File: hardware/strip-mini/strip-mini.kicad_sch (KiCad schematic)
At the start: 27 parts, among them J101 CORTEX-DEBUG, J102 JAE_DX07S016JA3, SW101 SW_Push, U101 AP2112K-3.3, U102 ATSAMD51G, Y101 32k768

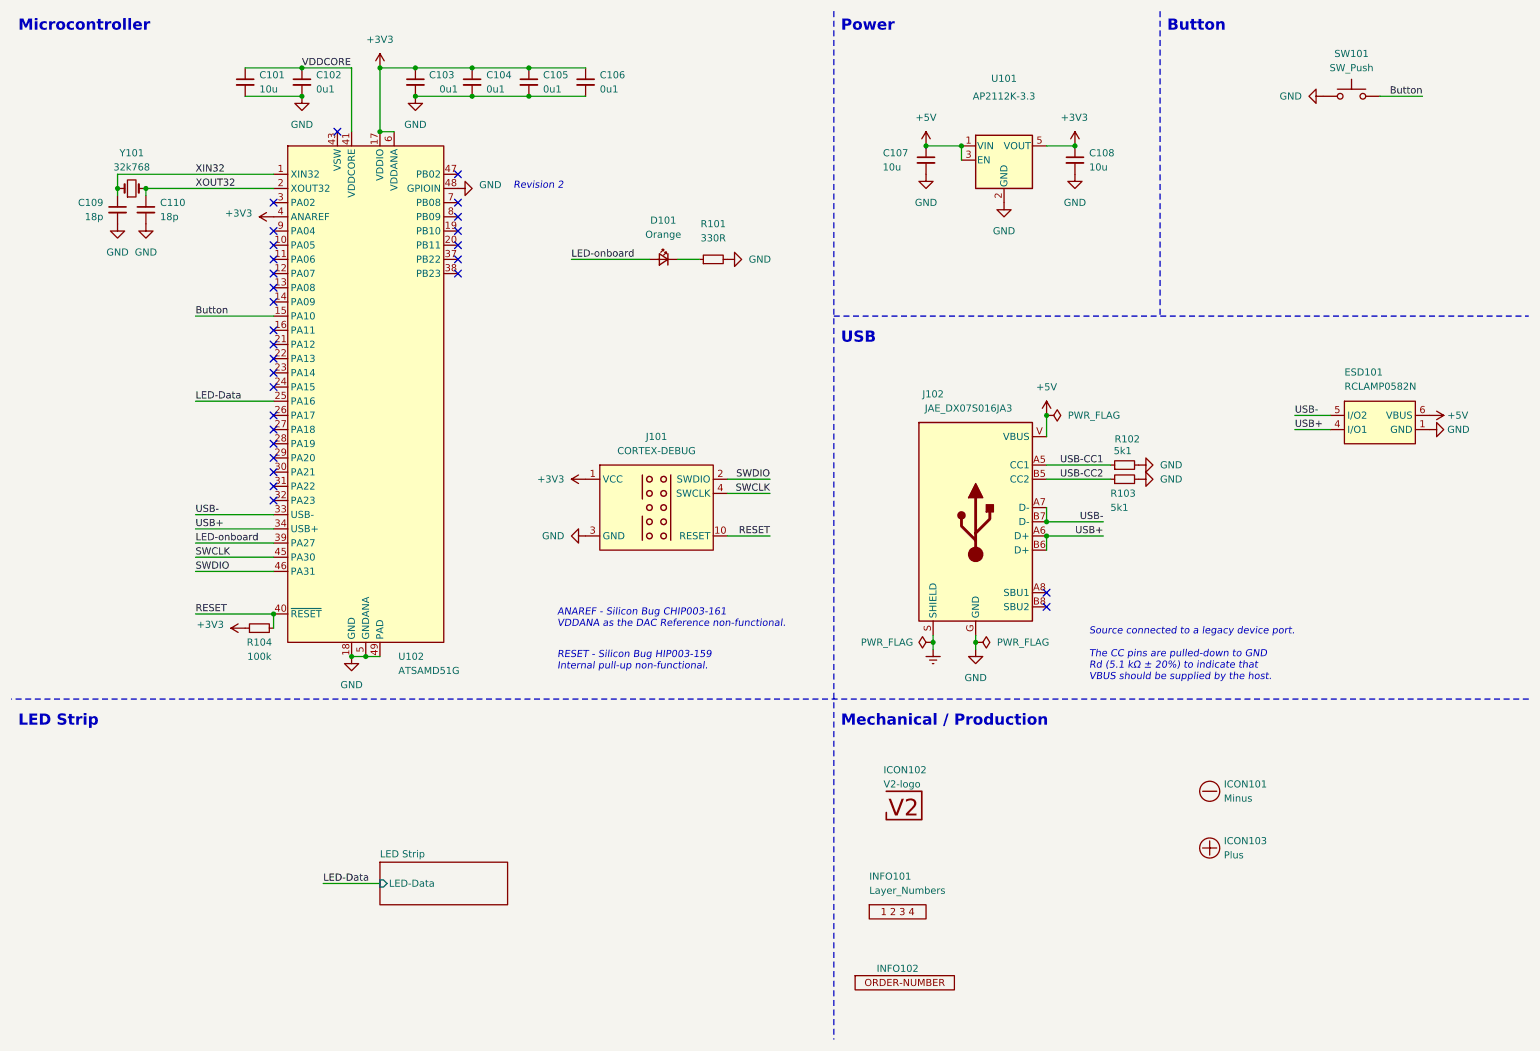
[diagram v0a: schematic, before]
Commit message: Replace Order_Number
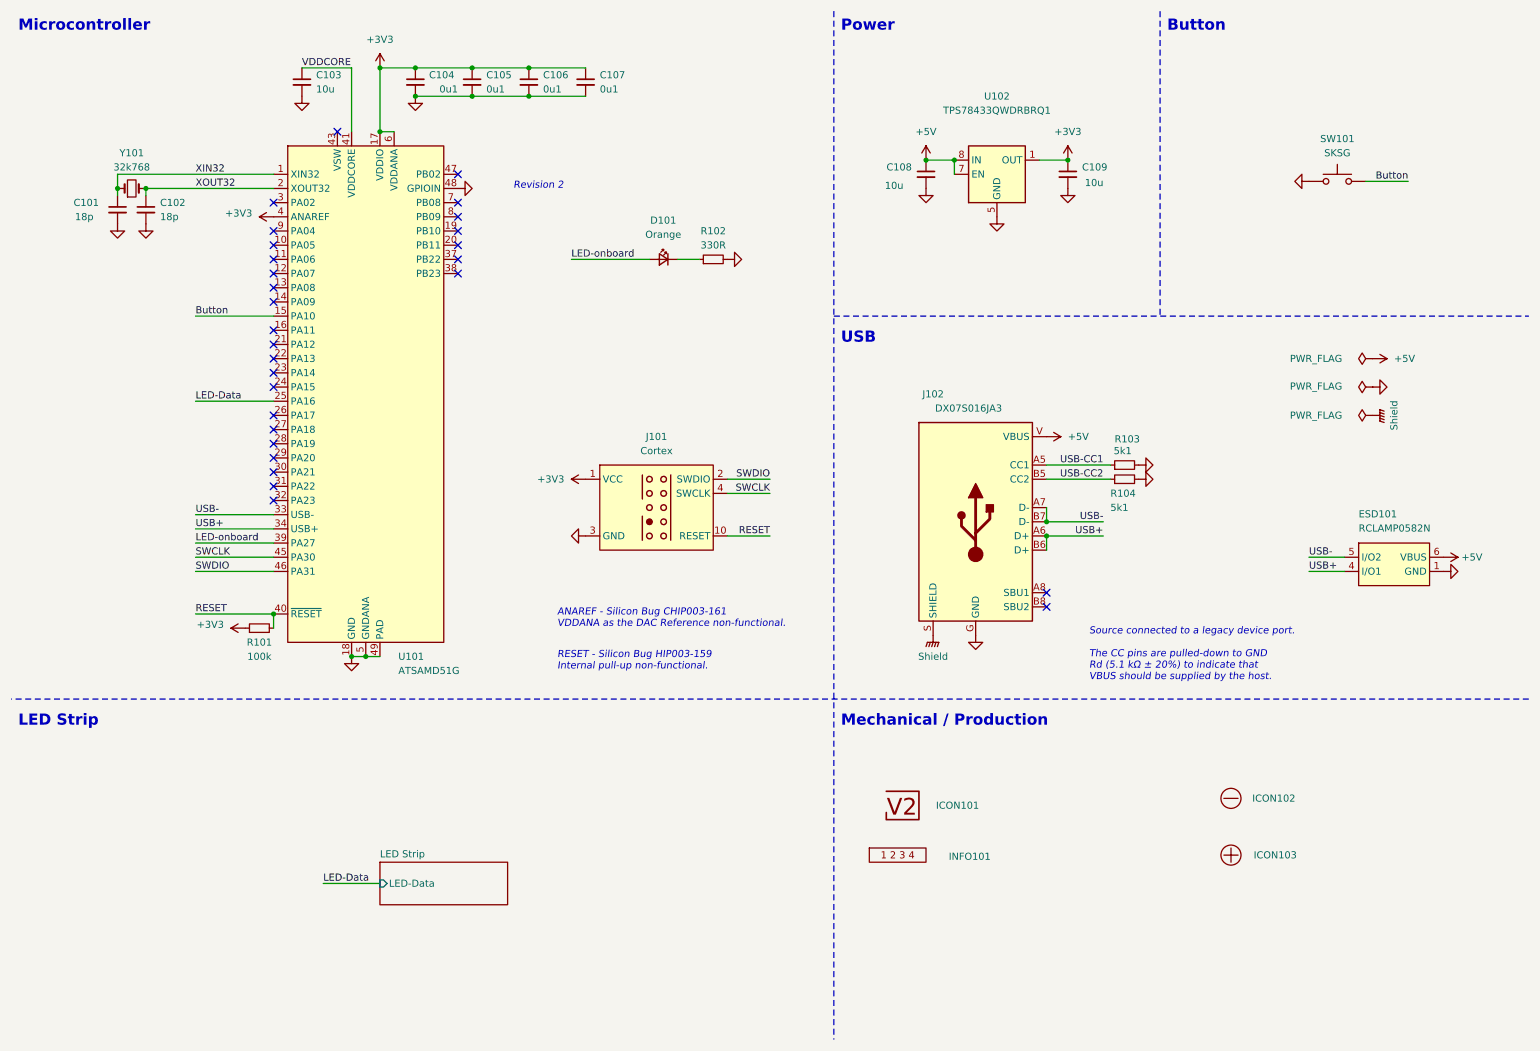
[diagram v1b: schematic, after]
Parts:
- removed C102: 0u1, Capacitor_SMD:C_0603_1608Metric, symbol Device:C_Small
- removed C107, C108: 10u, Capacitor_SMD:C_0603_1608Metric, symbol Device:C_Small
- removed INFO102: ORDER-NUMBER, V2_Production:Order_Number, symbol V2_Production:Order_Number
- removed U101: AP2112K-3.3, Package_TO_SOT_SMD:SOT-23-5, symbol Regulator_Linear:AP2112K-3.3
- added C108, C109: 10u, V2_Capacitor_SMD:C_0805, symbol V2_Device:C_0805_10u
- added U102: TPS78433QWDRBRQ1, V2_Package_SON:VSON-8-1_3x3mm_P0.65_EP1.65x2.4mm, symbol V2_Regulator_Linear:TPS78433QWDRBRQ1
- C101: renamed from C109; footprint Capacitor_SMD:C_0603_1608Metric -> V2_Capacitor_SMD:C_0603; symbol Device:C_Small -> V2_Device:C_0603_18p; Manufacturer (none) -> YAGEO; Mouser (none) -> 603-CC603JRNPO9BN180; Product (none) -> CC0603JRNPO9BN180
- C102: renamed from C110; footprint Capacitor_SMD:C_0603_1608Metric -> V2_Capacitor_SMD:C_0603; symbol Device:C_Small -> V2_Device:C_0603_18p; Manufacturer (none) -> YAGEO; Mouser (none) -> 603-CC603JRNPO9BN180; Product (none) -> CC0603JRNPO9BN180
- C103: renamed from C101; footprint Capacitor_SMD:C_0603_1608Metric -> V2_Capacitor_SMD:C_0603; symbol Device:C_Small -> V2_Device:C_0603_10u; Manufacturer (none) -> TDK; Mouser (none) -> 810-C1608X6S1A106M; Product (none) -> C1608X6S1A106M080AC; Rating (none) -> 10V
- C104: renamed from C103; footprint Capacitor_SMD:C_0603_1608Metric -> V2_Capacitor_SMD:C_0603; symbol Device:C_Small -> V2_Device:C_0603_0u1; Manufacturer (none) -> TDK; Mouser (none) -> 810-CGA3E2X7R1H104MA; Product (none) -> CGA3E2X7R1H104M080AA; Rating (none) -> 50V
- C105: renamed from C104; footprint Capacitor_SMD:C_0603_1608Metric -> V2_Capacitor_SMD:C_0603; symbol Device:C_Small -> V2_Device:C_0603_0u1; Manufacturer (none) -> TDK; Mouser (none) -> 810-CGA3E2X7R1H104MA; Product (none) -> CGA3E2X7R1H104M080AA; Rating (none) -> 50V
- C106: renamed from C105; footprint Capacitor_SMD:C_0603_1608Metric -> V2_Capacitor_SMD:C_0603; symbol Device:C_Small -> V2_Device:C_0603_0u1; Manufacturer (none) -> TDK; Mouser (none) -> 810-CGA3E2X7R1H104MA; Product (none) -> CGA3E2X7R1H104M080AA; Rating (none) -> 50V
- C107: renamed from C106; footprint Capacitor_SMD:C_0603_1608Metric -> V2_Capacitor_SMD:C_0603; symbol Device:C_Small -> V2_Device:C_0603_0u1; Manufacturer (none) -> TDK; Mouser (none) -> 810-CGA3E2X7R1H104MA; Product (none) -> CGA3E2X7R1H104M080AA; Rating (none) -> 50V
- D101: footprint LED_SMD:LED_0603_1608Metric -> V2_LED:LED_0603; symbol Device:LED_Small -> V2_Device:LED_0603_Orange; Manufacturer (none) -> ROHM Semiconductor; Mouser (none) -> 755-SML-D12D1WT86; Product (none) -> SML-D12D1WT86
- ESD101: Manufacturer (none) -> Semtech; Mouser (none) -> 947-RCLAMP0582N.TCT; Product (none) -> RCLAMP0582N.TCT
- ICON101: renamed from ICON102; symbol V2_Artwork:V2-logo -> V2_Artwork:V2-logo-tiny
- J101: value CORTEX-DEBUG -> Cortex; footprint V2_Cortex_Debug:Cortex_Debug_Pad -> V2_Connector_Debug:Cortex; symbol V2_Cortex_Debug:Cortex_Debug -> V2_Connector_Debug:Cortex
- J102: value JAE_DX07S016JA3 -> DX07S016JA3; Manufacturer (none) -> JAE Electronics; Mouser (none) -> 656-DX07S016JA3R1500; Product (none) -> DX07S016JA3R1500
- R101: renamed from R104; footprint Resistor_SMD:R_0603_1608Metric -> V2_Resistor_SMD:R_0603; symbol Device:R_Small -> V2_Device:R_0603_100k; Manufacturer (none) -> Vishay; Mouser (none) -> 71-CRCW0603100KFKEAC; Product (none) -> CRCW0603100KFKEAC; Rating (none) -> 100mW
- R102: renamed from R101; footprint Resistor_SMD:R_0603_1608Metric -> V2_Resistor_SMD:R_0603; symbol Device:R_Small -> V2_Device:R_0603_330R; Manufacturer (none) -> Vishay; Mouser (none) -> 71-CRCW0603330RFKEAC; Product (none) -> CRCW0603330RFKEAC; Rating (none) -> 100mW
- R103: renamed from R102; footprint Resistor_SMD:R_0603_1608Metric -> V2_Resistor_SMD:R_0603; symbol Device:R_Small -> V2_Device:R_0603_5k1; Manufacturer (none) -> Vishay; Mouser (none) -> 71-CRCW06035K10FKEAC; Product (none) -> CRCW06035K10FKEAC; Rating (none) -> 100mW
- R104: renamed from R103; footprint Resistor_SMD:R_0603_1608Metric -> V2_Resistor_SMD:R_0603; symbol Device:R_Small -> V2_Device:R_0603_5k1; Manufacturer (none) -> Vishay; Mouser (none) -> 71-CRCW06035K10FKEAC; Product (none) -> CRCW06035K10FKEAC; Rating (none) -> 100mW
- SW101: value SW_Push -> SKSG; symbol Switch:SW_Push -> V2_Switch:SKSG; Manufacturer (none) -> Alps Alpine; Mouser (none) -> 688-SKSGACE010; Product (none) -> SKSGACE010
- U101: renamed from U102; Manufacturer (none) -> Microchip Technology; Mouser (none) -> 556-ATSAMD51G19AMU; Product (none) -> ATSAMD51G19A-MU
- Y101: symbol Device:Crystal_Small -> V2_Device:Crystal_3.2x1.5_32k768; Manufacturer (none) -> ABRACON; Mouser (none) -> 815-ABS0716632.768KT; Product (none) -> ABS07-166-32.768KHZ-T
- renumbered ICON101 to ICON102
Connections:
- net +3V3: now also C109.1, U102.1 (OUT)
- net +5V: now also C108.1, U102.7 (EN), U102.8 (IN)
- net GND: now also C108.2, C109.2, U102.5 (GND), U102.9 (GND)
- net Earth renamed Shield
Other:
- moved on the sheet: C103, ESD101, ICON102, ICON103, INFO101, SW101

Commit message: Update Library
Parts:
- C101, C102: symbol V2_Device:C_0603_18p -> V2_Capacitor:0603_18p
- C103: symbol V2_Device:C_0603_10u -> V2_Capacitor:0603_10u
- C104, C105, C106, C107: symbol V2_Device:C_0603_0u1 -> V2_Capacitor:0603_0u1
- C108, C109: symbol V2_Device:C_0805_10u -> V2_Capacitor:0805_10u
- D101: symbol V2_Device:LED_0603_Orange -> V2_LED:0603_Orange
- R101: symbol V2_Device:R_0603_100k -> V2_Resistor:0603_100k
- R102: symbol V2_Device:R_0603_330R -> V2_Resistor:0603_330R
- R103, R104: symbol V2_Device:R_0603_5k1 -> V2_Resistor:0603_5k1
- Y101: symbol V2_Device:Crystal_3.2x1.5_32k768 -> V2_Crystal:3.2x1.5_32k768

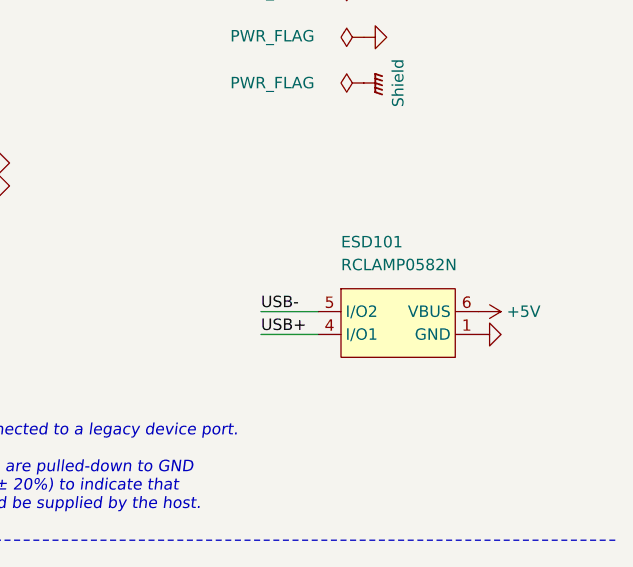
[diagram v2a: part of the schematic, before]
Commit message: Update ESD suppressor
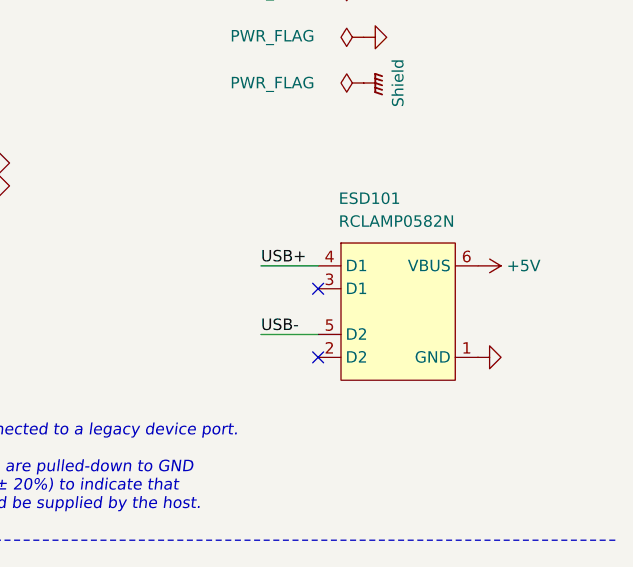
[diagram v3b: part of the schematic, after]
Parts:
- C101, C102: Manufacturer YAGEO -> TDK; Mouser 603-CC603JRNPO9BN180 -> 810-CGA3E2C0G1H180J; Product CC0603JRNPO9BN180 -> CGA3E2C0G1H180J080AA
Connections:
- no-connect marks 29 -> 31
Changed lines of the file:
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@@
 	(title_block
 		(title "V2 strip mini")
-		(date "2026-02-11")
+		(date "2026-03-14")
 		(rev "2026-02-11")
 		(company "Versio Duo")
@@
 	)
 	(no_connect
+		(at 251.46 115.57)
+	)
+	(no_connect
+		(at 251.46 107.95)
+	)
+	(no_connect
 		(at 71.12 34.29)
 	)
@@
 	(wire
 		(pts
-			(xy 245.11 110.49) (xy 251.46 110.49)
+			(xy 245.11 113.03) (xy 251.46 113.03)
 		)
 		(stroke
@@
 		)
 	)
+	(wire
+		(pts
+			(xy 245.11 105.41) (xy 251.46 105.41)
+		)
+		(stroke
+			(width 0)
+			(type default)
+		)
+	)
 	(polyline
 		(pts
@@
 	(wire
 		(pts
-			(xy 245.11 113.03) (xy 251.46 113.03)
-		)
-		(stroke
-			(width 0)
-			(type default)
-		)
-	)
-	(wire
-		(pts
 			(xy 113.03 57.15) (xy 127 57.15)
 		)
@@
 	)
 	(label "USB+"
+		(at 245.11 105.41 0)
+		(effects
+			(font
+				(size 1.27 1.27)
+			)
+			(justify left bottom)
+		)
+	)
+	(label "USB+"
 		(at 45.72 105.41 0)
 		(effects
@@
 		)
 	)
-	(label "USB+"
-		(at 245.11 113.03 0)
-		(effects
-			(font
-				(size 1.27 1.27)
-			)
-			(justify left bottom)
-		)
-	)
 	(label "SWDIO"
 		(at 148.59 96.52 180)
@@
 	)
 	(label "USB-"
-		(at 245.11 110.49 0)
+		(at 245.11 113.03 0)
 		(effects
 			(font
@@
 			)
 		)
-		(property "Description" "Resistor, small symbol"
+		(property "Description" ""
 			(at 224.79 93.98 0)
 			(effects
@@
 			)
 		)
-		(property "Description" "Unpolarized capacitor, small symbol"
+		(property "Description" ""
 			(at 115.57 38.1 0)
 			(effects
@@
 		(dnp no)
 		(property "Reference" "ESD101"
-			(at 254 103.505 0)
+			(at 253.746 98.679 0)
 			(effects
 				(font
@@
 		)
 		(property "Value" "RCLAMP0582N"
-			(at 254 106.045 0)
+			(at 253.746 101.219 0)
 			(effects
 				(font
@@
 			)
 		)
-		(property "Description" "Push button switch, generic, two pins"
+		(property "Description" "Push button"
 			(at 250.19 43.18 0)
 			(effects
@@
 	(symbol
 		(lib_id "V2_power:+5V")
-		(at 269.24 110.49 270)
+		(at 269.24 105.41 270)
 		(unit 1)
 		(exclude_from_sim no)
@@
 		(fields_autoplaced yes)
 		(property "Reference" "#PWR127"
-			(at 265.43 110.49 0)
+			(at 265.43 105.41 0)
 			(effects
 				(font
@@
 		)
 		(property "Value" "+5V"
-			(at 272.415 110.4899 90)
+			(at 272.415 105.4099 90)
 			(effects
 				(font
@@
 		)
 		(property "Footprint" ""
-			(at 269.24 110.49 0)
+			(at 269.24 105.41 0)
 			(effects
 				(font
@@
 		)
 		(property "Datasheet" ""
-			(at 269.24 110.49 0)
+			(at 269.24 105.41 0)
 			(effects
 				(font
@@
 		)
 		(property "Description" ""
-			(at 269.24 110.49 0)
+			(at 269.24 105.41 0)
 			(effects
 				(font
@@
 			)
 		)
-		(property "Description" "Light emitting diode, small symbol"
+		(property "Description" ""
 			(at 129.54 57.15 0)
 			(effects
@@
 			)
 		)
-		(property "Description" "Unpolarized capacitor, small symbol"
+		(property "Description" ""
 			(at 176.53 55.372 0)
 			(effects
@@
 			)
 		)
-		(property "Description" "Two pin crystal, small symbol"
+		(property "Description" ""
 			(at 34.29 44.45 0)
 			(effects
@@
 			)
 		)
-		(property "Description" "Unpolarized capacitor, small symbol"
+		(property "Description" ""
 			(at 36.83 62.738 0)
 			(effects
@@
 			)
 		)
-		(property "Mouser" "603-CC603JRNPO9BN180"
+		(property "Mouser" "810-CGA3E2C0G1H180J"
 			(at 36.83 71.628 0)
 			(effects
@@
 			)
 		)
-		(property "Product" "CC0603JRNPO9BN180"
+		(property "Product" "CGA3E2C0G1H180J080AA"
 			(at 36.83 68.834 0)
 			(effects
@@
 			)
 		)
-		(property "Manufacturer" "YAGEO"
+		(property "Manufacturer" "TDK"
 			(at 36.83 66.04 0)
 			(effects
@@
 			)
 		)
-		(property "Description" "Unpolarized capacitor, small symbol"
+		(property "Description" ""
 			(at 64.77 40.64 0)
 			(effects
@@
 			)
 		)
-		(property "Description" "Unpolarized capacitor, small symbol"
+		(property "Description" ""
 			(at 31.75 62.738 0)
 			(effects
@@
 			)
 		)
-		(property "Mouser" "603-CC603JRNPO9BN180"
+		(property "Mouser" "810-CGA3E2C0G1H180J"
 			(at 31.75 71.628 0)
 			(effects
@@
 			)
 		)
-		(property "Product" "CC0603JRNPO9BN180"
+		(property "Product" "CGA3E2C0G1H180J080AA"
 			(at 31.75 68.834 0)
 			(effects
@@
 			)
 		)
-		(property "Manufacturer" "YAGEO"
+		(property "Manufacturer" "TDK"
 			(at 31.75 66.04 0)
 			(effects
@@
 			)
 		)
-		(property "Description" "Resistor, small symbol"
+		(property "Description" ""
 			(at 151.13 57.15 0)
 			(effects
@@
 	(symbol
 		(lib_id "V2_power:GND")
-		(at 269.24 113.03 90)
+		(at 269.24 115.57 90)
 		(unit 1)
 		(exclude_from_sim no)
@@
 		(fields_autoplaced yes)
 		(property "Reference" "#PWR128"
-			(at 275.59 113.03 0)
+			(at 275.59 115.57 0)
 			(effects
 				(font
@@
 		)
 		(property "Value" "GND"
-			(at 272.415 113.0299 90)
+			(at 272.415 115.5699 90)
 			(effects
 				(font
@@
 		)
 		(property "Footprint" ""
-			(at 269.24 113.03 0)
+			(at 269.24 115.57 0)
 			(effects
 				(font
@@
 		)
 		(property "Datasheet" ""
-			(at 269.24 113.03 0)
+			(at 269.24 115.57 0)
 			(effects
 				(font
@@
 		)
 		(property "Description" ""
-			(at 269.24 113.03 0)
+			(at 269.24 115.57 0)
 			(effects
 				(font
@@
 			)
 		)
-		(property "Description" "Unpolarized capacitor, small symbol"
+		(property "Description" ""
 			(at 105.41 38.1 0)
 			(effects
@@
 			)
 		)
-		(property "Description" "Unpolarized capacitor, small symbol"
+		(property "Description" ""
 			(at 201.93 55.372 0)
 			(effects
@@
 			)
 		)
-		(property "Description" "Unpolarized capacitor, small symbol"
+		(property "Description" ""
 			(at 85.09 38.1 0)
 			(effects
@@
 			)
 		)
-		(property "Description" "Resistor, small symbol"
+		(property "Description" ""
 			(at 224.79 96.52 0)
 			(effects
@@
 			)
 		)
-		(property "Description" "Unpolarized capacitor, small symbol"
+		(property "Description" ""
 			(at 95.25 38.1 0)
 			(effects
@@
 			)
 		)
-		(property "Description" "Resistor, small symbol"
+		(property "Description" ""
 			(at 69.85 123.19 0)
 			(effects

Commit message: Update
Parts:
- C101, C102: Id (none) -> Capacitor:${SYMBOL_NAME}; Rating (none) -> 50V
- C103, C104, C105, C106, C107, C108, C109: Id (none) -> Capacitor:${SYMBOL_NAME}
- D101: Id (none) -> LED:${SYMBOL_NAME}; Rating (none) -> 605nm
- ESD101: Id (none) -> ESD:${SYMBOL_NAME}; Rating (none) -> 20kV
- J102: Id (none) -> USB:${SYMBOL_NAME}; Rating (none) -> USB2.0
- R101, R102, R103, R104: Id (none) -> Resistor:${SYMBOL_NAME}
- SW101: Id (none) -> Button:${SYMBOL_NAME}; Rating (none) -> 1.6N
- U101: Id (none) -> MCU:${SYMBOL_NAME}; Rating (none) -> Cortex-M4F
- U102: Id (none) -> LDO:${SYMBOL_NAME}; Rating (none) -> 300mA
- Y101: Id (none) -> Crystal:${SYMBOL_NAME}; Rating (none) -> 10ppm
